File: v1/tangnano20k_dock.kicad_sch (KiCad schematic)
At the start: 42 parts, among them J1 Mini-DIN-6, J2 2x20 Pin Female, J3 Conn_01x03_Male, J4 Conn_01x20, J5 Conn_01x02, J6 RCA, J7 FCR684205T, J8 AudioJack3, U1 TXS0104E, U2 TangNano20K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

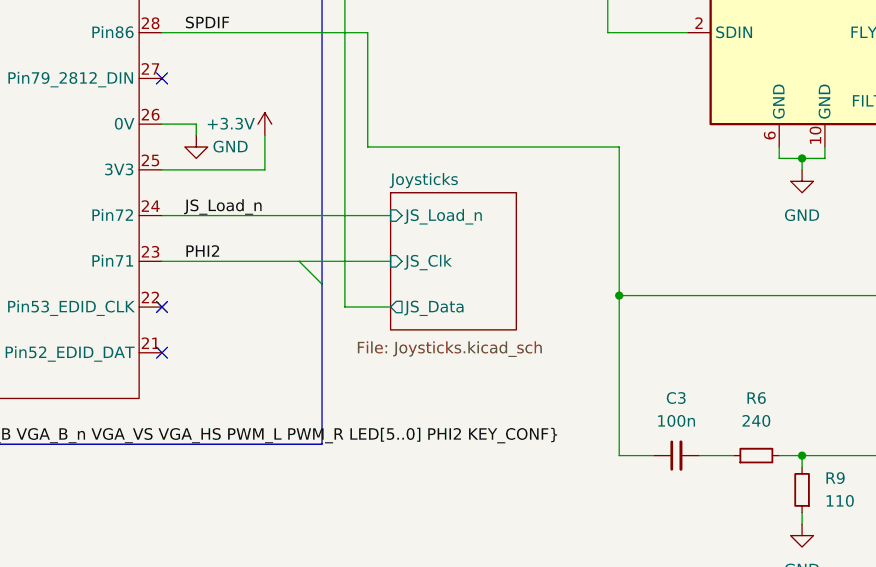
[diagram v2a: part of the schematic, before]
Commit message: Add an RC filter to allow PHI2 clock edge to be slowed to avoid ringing
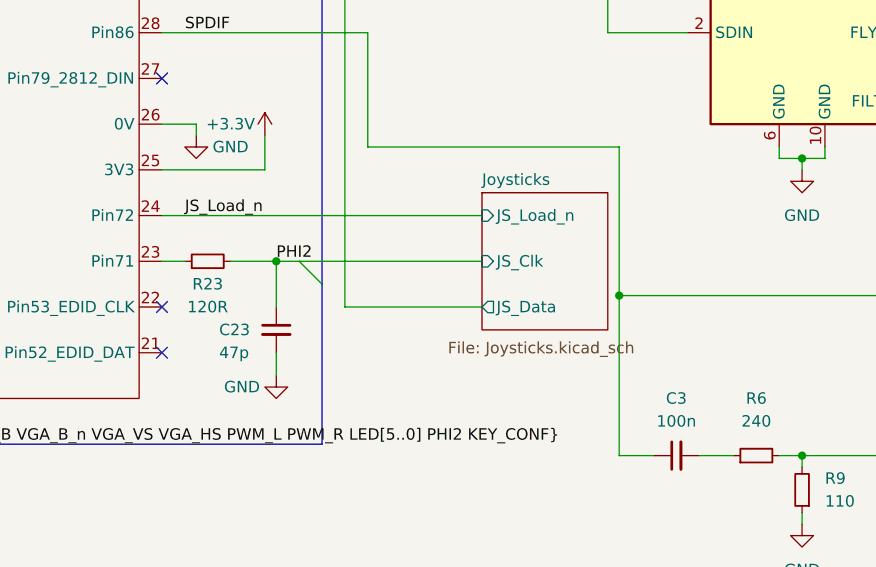
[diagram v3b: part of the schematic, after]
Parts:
- added C23: 47p, Capacitor_SMD:C_1206_3216Metric_Pad1.33x1.80mm_HandSolder, symbol Device:C_Small
- added R23: 120R, Resistor_SMD:R_1206_3216Metric_Pad1.30x1.75mm_HandSolder, symbol Device:R_Small
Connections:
- net GND: now also C23.2
- net PHI2: now also C23.1, R23.2; no longer U2.23 (Pin71)
- new net: R23.1, U2.23 (Pin71)
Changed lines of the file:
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@@
   (junction (at 250.19 73.66) (diameter 0) (color 0 0 0 0)
   )
+  (junction (at 173.99 130.81) (diameter 0) (color 0 0 0 0)
+  )
   (junction (at 107.95 151.13) (diameter 0) (color 0 0 0 0)
   )
@@
     (stroke (width 0) (type default) (color 0 0 0 0))
   )
+  (wire (pts (xy 161.29 130.81) (xy 163.83 130.81))
+    (stroke (width 0) (type default) (color 0 0 0 0))
+  )
   (wire (pts (xy 267.97 144.78) (xy 267.97 146.05))
     (stroke (width 0) (type default) (color 0 0 0 0))
@@
     (stroke (width 0) (type default) (color 0 0 0 0))
   )
-  (wire (pts (xy 181.61 135.89) (xy 186.69 135.89))
+  (wire (pts (xy 181.61 135.89) (xy 196.85 135.89))
     (stroke (width 0) (type default) (color 0 0 0 0))
   )
@@
     (stroke (width 0) (type default) (color 0 0 0 0))
   )
-  (wire (pts (xy 161.29 130.81) (xy 176.53 130.81))
-    (stroke (width 0) (type default) (color 0 0 0 0))
-  )
   (bus (pts (xy 39.37 97.79) (xy 39.37 100.33))
     (stroke (width 0) (type default) (color 0 0 0 0))
@@
     (stroke (width 0) (type default) (color 0 0 0 0))
   )
-  (wire (pts (xy 176.53 130.81) (xy 186.69 130.81))
+  (wire (pts (xy 176.53 130.81) (xy 196.85 130.81))
     (stroke (width 0) (type default) (color 0 0 0 0))
   )
@@
     (stroke (width 0) (type default) (color 0 0 0 0))
   )
+  (wire (pts (xy 168.91 130.81) (xy 173.99 130.81))
+    (stroke (width 0) (type default) (color 0 0 0 0))
+  )
   (wire (pts (xy 64.77 85.09) (xy 54.61 85.09))
     (stroke (width 0) (type default) (color 0 0 0 0))
@@
     (stroke (width 0) (type default) (color 0 0 0 0))
   )
+  (wire (pts (xy 173.99 140.97) (xy 173.99 143.51))
+    (stroke (width 0) (type default) (color 0 0 0 0))
+  )
   (wire (pts (xy 250.19 67.31) (xy 250.19 66.04))
     (stroke (width 0) (type default) (color 0 0 0 0))
@@
     (stroke (width 0) (type default) (color 0 0 0 0))
   )
+  (wire (pts (xy 173.99 135.89) (xy 173.99 130.81))
+    (stroke (width 0) (type default) (color 0 0 0 0))
+  )
   (wire (pts (xy 212.09 152.4) (xy 215.9 152.4))
     (stroke (width 0) (type default) (color 0 0 0 0))
@@
     (stroke (width 0) (type default) (color 0 0 0 0))
   )
+  (wire (pts (xy 173.99 130.81) (xy 176.53 130.81))
+    (stroke (width 0) (type default) (color 0 0 0 0))
+  )
   (bus (pts (xy 107.95 118.11) (xy 107.95 123.19))
     (stroke (width 0) (type default) (color 0 0 0 0))
@@
     (stroke (width 0) (type default) (color 0 0 0 0))
   )
-  (wire (pts (xy 161.29 125.73) (xy 186.69 125.73))
+  (wire (pts (xy 161.29 125.73) (xy 196.85 125.73))
     (stroke (width 0) (type default) (color 0 0 0 0))
   )
@@
     (effects (font (size 1.27 1.27)) (justify left bottom))
   )
-  (label "PHI2" (at 163.83 130.81 0)
+  (label "PHI2" (at 173.99 130.81 0)
     (effects (font (size 1.27 1.27)) (justify left bottom))
   )
@@
     (pin "2")
   )
+  (symbol (lib_id "Device:C_Small") (at 173.99 138.43 0) (unit 1)
+    (in_bom yes) (on_board yes)
+    (property "Reference" "C23" (id 0) (at 167.64 138.43 0)
+      (effects (font (size 1.27 1.27)) (justify left))
+    )
+    (property "Value" "47p" (id 1) (at 167.64 140.97 0)
+      (effects (font (size 1.27 1.27)) (justify left))
+    )
+    (property "Footprint" "Capacitor_SMD:C_1206_3216Metric_Pad1.33x1.80mm_HandSolder" (id 2) (at 173.99 138.43 0)
+      (effects (font (size 1.27 1.27)) hide)
+    )
+    (property "Datasheet" "~" (id 3) (at 173.99 138.43 0)
+      (effects (font (size 1.27 1.27)) hide)
+    )
+    (pin "1")
+    (pin "2")
+  )
   (symbol (lib_id "Device:C_Small") (at 74.93 19.05 0) (mirror x) (unit 1)
     (in_bom yes) (on_board yes)
@@
     (pin "1")
   )
+  (symbol (lib_id "Device:R_Small") (at 166.37 130.81 90) (unit 1)
+    (in_bom yes) (on_board yes)
+    (property "Reference" "R23" (id 0) (at 166.37 133.35 90))
+    (property "Value" "120R" (id 1) (at 166.37 135.89 90))
+    (property "Footprint" "Resistor_SMD:R_1206_3216Metric_Pad1.30x1.75mm_HandSolder" (id 2) (at 166.37 130.81 0)
+      (effects (font (size 1.27 1.27)) hide)
+    )
+    (property "Datasheet" "~" (id 3) (at 166.37 130.81 0)
+      (effects (font (size 1.27 1.27)) hide)
+    )
+    (pin "1")
+    (pin "2")
+  )
   (symbol (lib_id "power:GND") (at 232.41 120.65 0) (unit 1)
     (in_bom yes) (on_board yes) (fields_autoplaced)
@@
     (pin "3")
   )
+  (symbol (lib_id "power:GND") (at 173.99 143.51 0) (unit 1)
+    (in_bom yes) (on_board yes)
+    (property "Reference" "#PWR0101" (id 0) (at 173.99 149.86 0)
+      (effects (font (size 1.27 1.27)) hide)
+    )
+    (property "Value" "GND" (id 1) (at 170.18 144.78 0))
+    (property "Footprint" "" (id 2) (at 173.99 143.51 0)
+      (effects (font (size 1.27 1.27)) hide)
+    )
+    (property "Datasheet" "" (id 3) (at 173.99 143.51 0)
+      (effects (font (size 1.27 1.27)) hide)
+    )
+    (pin "1")
+  )
   (symbol (lib_id "Mechanical:MountingHole") (at 185.42 34.29 0) (unit 1)
     (in_bom yes) (on_board yes) (fields_autoplaced)
@@
     (pin "1")
   )
-  (sheet (at 186.69 123.19) (size 13.97 15.24)
+  (sheet (at 196.85 123.19) (size 13.97 15.24)
     (stroke (width 0.1524) (type solid) (color 0 0 0 0))
     (fill (color 0 0 0 0.0000))
-    (property "Sheet name" "Joysticks" (id 0) (at 186.69 122.4784 0)
+    (property "Sheet name" "Joysticks" (id 0) (at 196.85 122.4784 0)
       (effects (font (size 1.27 1.27)) (justify left bottom))
     )
-    (property "Sheet file" "Joysticks.kicad_sch" (id 1) (at 182.88 139.7 0)
+    (property "Sheet file" "Joysticks.kicad_sch" (id 1) (at 193.04 139.7 0)
       (effects (font (size 1.27 1.27)) (justify left top))
     )
-    (pin "JS_Data" output (at 186.69 135.89 180)
+    (pin "JS_Data" output (at 196.85 135.89 180)
       (effects (font (size 1.27 1.27)) (justify left))
     )
-    (pin "JS_Load_n" input (at 186.69 125.73 180)
+    (pin "JS_Load_n" input (at 196.85 125.73 180)
       (effects (font (size 1.27 1.27)) (justify left))
     )
-    (pin "JS_Clk" input (at 186.69 130.81 180)
+    (pin "JS_Clk" input (at 196.85 130.81 180)
       (effects (font (size 1.27 1.27)) (justify left))
     )
@@
       (reference "#PWR055") (unit 1) (value "GND") (footprint "")
     )
+    (path "/7eb3d7a6-25d3-48be-8262-4dda673731da"
+      (reference "#PWR0101") (unit 1) (value "GND") (footprint "")
+    )
     (path "/1fd682e2-38d3-4e6f-9b3a-e87d3b2b467c"
       (reference "C1") (unit 1) (value "100n") (footprint "Capacitor_SMD:C_1206_3216Metric_Pad1.33x1.80mm_HandSolder")
@@
       (reference "C22") (unit 1) (value "100n") (footprint "Capacitor_SMD:C_1206_3216Metric_Pad1.33x1.80mm_HandSolder")
     )
+    (path "/1b77f8d4-06d7-4df1-a443-7f89e552bd40"
+      (reference "C23") (unit 1) (value "47p") (footprint "Capacitor_SMD:C_1206_3216Metric_Pad1.33x1.80mm_HandSolder")
+    )
     (path "/3efa4c66-1bea-40a4-bda9-02b28c07af29"
       (reference "H1") (unit 1) (value "MountingHole") (footprint "TangNano20k:MountingHole_3.2mm_M3")
@@
       (reference "R22") (unit 1) (value "100") (footprint "Resistor_SMD:R_1206_3216Metric_Pad1.30x1.75mm_HandSolder")
     )
+    (path "/21ede51c-808e-4d97-ae44-af346bb9dd2e"
+      (reference "R23") (unit 1) (value "120R") (footprint "Resistor_SMD:R_1206_3216Metric_Pad1.30x1.75mm_HandSolder")
+    )
     (path "/0331ec4d-b3bf-4145-9efb-ad1204df77fa/8258306a-00ac-4756-af11-954dcf664468"

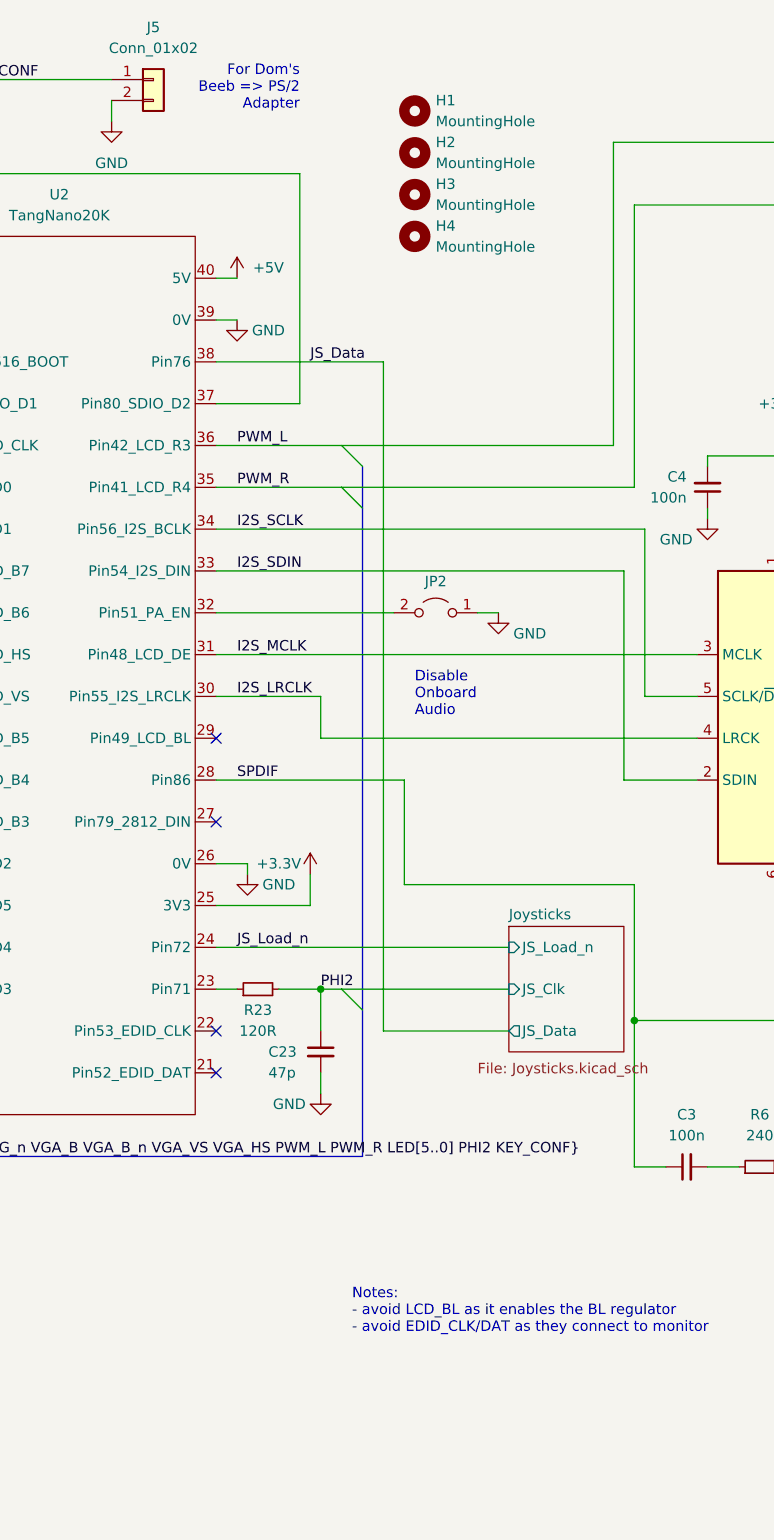
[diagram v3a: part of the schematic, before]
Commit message: Added Cliff DC10A power jack + schottky diode
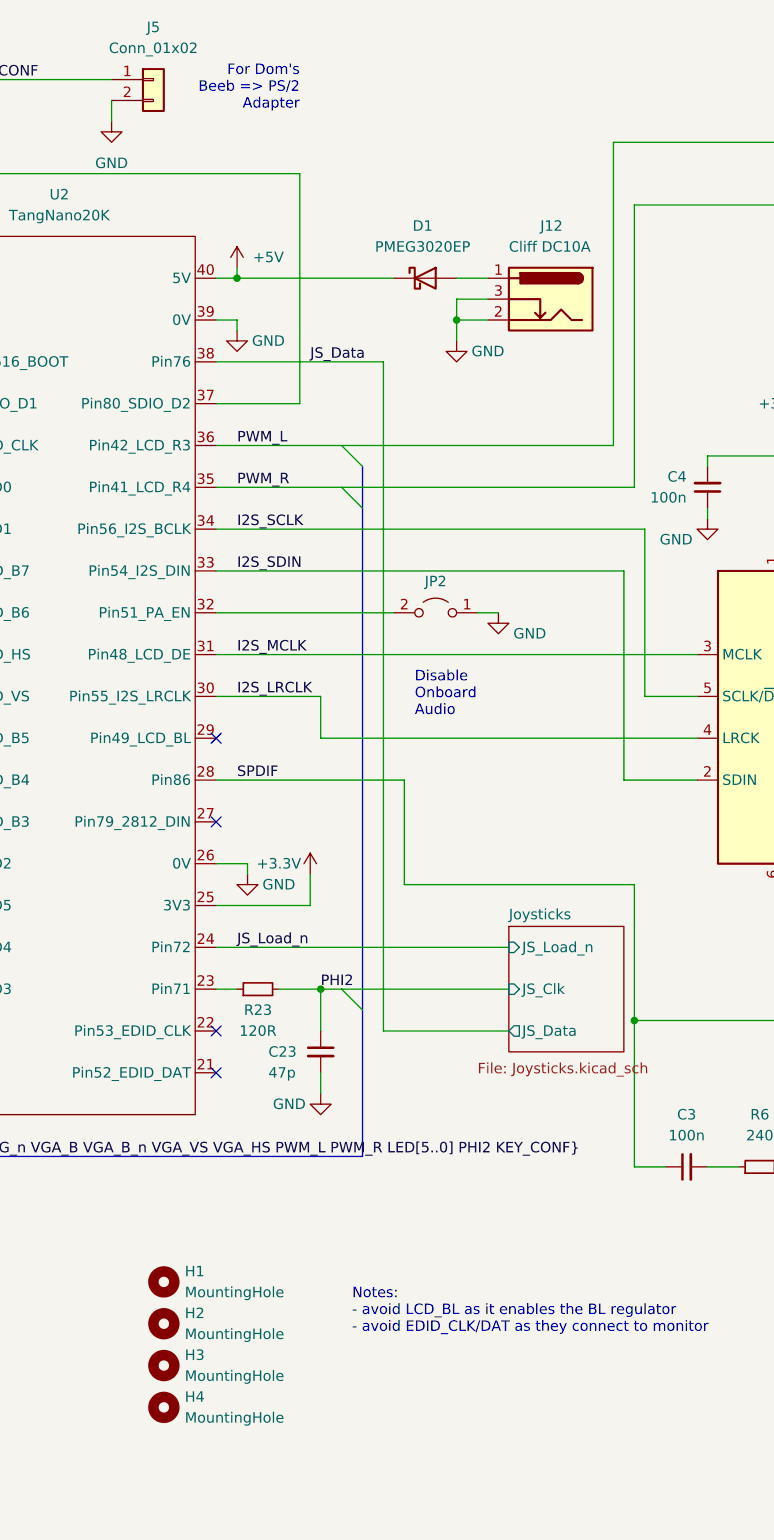
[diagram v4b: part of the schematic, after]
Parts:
- added D1: PMEG3020EP, Diode_SMD:D_SOD-128, symbol Device:D_Schottky
- added J12: Cliff DC10A, TangNano20k:CLIFF_FC68148_DC10A, symbol Connector:Barrel_Jack_Switch
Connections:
- net +5V: now also D1.1 (K)
- net GND: now also J12.2, J12.3
- new net: D1.2 (A), J12.1
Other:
- moved on the sheet: H1, H2, H3, H4

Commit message: More minor DFM issues
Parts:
- D1: footprint Diode_SMD:D_SOD-128 -> TangNano20k:D_SOD-128
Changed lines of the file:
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@@
     (property "Reference" "D1" (id 0) (at 186.3725 38.1 0))
     (property "Value" "PMEG3020EP" (id 1) (at 186.3725 40.64 0))
-    (property "Footprint" "Diode_SMD:D_SOD-128" (id 2) (at 186.69 44.45 0)
+    (property "Footprint" "TangNano20k:D_SOD-128" (id 2) (at 186.69 44.45 0)
       (effects (font (size 1.27 1.27)) hide)
     )
@@
     )
     (path "/23e0812c-8650-479d-a1a6-e0d5388e06e9"
-      (reference "D1") (unit 1) (value "PMEG3020EP") (footprint "Diode_SMD:D_SOD-128")
+      (reference "D1") (unit 1) (value "PMEG3020EP") (footprint "TangNano20k:D_SOD-128")
     )
     (path "/3efa4c66-1bea-40a4-bda9-02b28c07af29"

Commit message: Update resistor values and refresh PDF
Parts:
- R1, R2, R3, R4: value 390 -> 330
- R23: value 120R -> 100R
- R5: value 10K -> 3K3
- R6: value 240 -> 243
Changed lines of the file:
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@@
       (effects (font (size 1.27 1.27)) (justify left))
     )
-    (property "Value" "10K" (id 1) (at 109.22 26.6699 0)
+    (property "Value" "3K3" (id 1) (at 109.22 26.6699 0)
       (effects (font (size 1.27 1.27)) (justify left))
     )
@@
     (in_bom yes) (on_board yes)
     (property "Reference" "R23" (id 0) (at 166.37 133.35 90))
-    (property "Value" "120R" (id 1) (at 166.37 135.89 90))
+    (property "Value" "100R" (id 1) (at 166.37 135.89 90))
     (property "Footprint" "Resistor_SMD:R_1206_3216Metric_Pad1.30x1.75mm_HandSolder" (id 2) (at 166.37 130.81 0)
       (effects (font (size 1.27 1.27)) hide)
@@
     (in_bom yes) (on_board yes) (fields_autoplaced)
     (property "Reference" "R6" (id 0) (at 227.33 146.05 90))
-    (property "Value" "240" (id 1) (at 227.33 148.59 90))
+    (property "Value" "243" (id 1) (at 227.33 148.59 90))
     (property "Footprint" "Resistor_SMD:R_1206_3216Metric_Pad1.30x1.75mm_HandSolder" (id 2) (at 227.33 152.4 0)
       (effects (font (size 1.27 1.27)) hide)
@@
     (in_bom yes) (on_board yes)
     (property "Reference" "R1" (id 0) (at 50.8 26.67 90))
-    (property "Value" "390" (id 1) (at 50.8 21.59 90))
+    (property "Value" "330" (id 1) (at 50.8 21.59 90))
     (property "Footprint" "Resistor_SMD:R_1206_3216Metric_Pad1.30x1.75mm_HandSolder" (id 2) (at 50.8 24.13 0)
       (effects (font (size 1.27 1.27)) hide)
@@
     (in_bom yes) (on_board yes)
     (property "Reference" "R4" (id 0) (at 50.8 62.23 90))
-    (property "Value" "390" (id 1) (at 50.8 57.15 90))
+    (property "Value" "330" (id 1) (at 50.8 57.15 90))
     (property "Footprint" "Resistor_SMD:R_1206_3216Metric_Pad1.30x1.75mm_HandSolder" (id 2) (at 50.8 59.69 0)
       (effects (font (size 1.27 1.27)) hide)
@@
     (in_bom yes) (on_board yes)
     (property "Reference" "R3" (id 0) (at 50.8 54.61 90))
-    (property "Value" "390" (id 1) (at 50.8 49.53 90))
+    (property "Value" "330" (id 1) (at 50.8 49.53 90))
     (property "Footprint" "Resistor_SMD:R_1206_3216Metric_Pad1.30x1.75mm_HandSolder" (id 2) (at 50.8 52.07 0)
       (effects (font (size 1.27 1.27)) hide)
@@
     (in_bom yes) (on_board yes)
     (property "Reference" "R2" (id 0) (at 50.8 34.29 90))
-    (property "Value" "390" (id 1) (at 50.8 29.21 90))
+    (property "Value" "330" (id 1) (at 50.8 29.21 90))
     (property "Footprint" "Resistor_SMD:R_1206_3216Metric_Pad1.30x1.75mm_HandSolder" (id 2) (at 50.8 31.75 0)
       (effects (font (size 1.27 1.27)) hide)
@@
     )
     (path "/4dc74927-f9a9-448a-9b80-6c4062674486"
-      (reference "R1") (unit 1) (value "390") (footprint "Resistor_SMD:R_1206_3216Metric_Pad1.30x1.75mm_HandSolder")
+      (reference "R1") (unit 1) (value "330") (footprint "Resistor_SMD:R_1206_3216Metric_Pad1.30x1.75mm_HandSolder")
     )
     (path "/d9474aa6-7130-4a20-8e60-ca64b8599c1b"
-      (reference "R2") (unit 1) (value "390") (footprint "Resistor_SMD:R_1206_3216Metric_Pad1.30x1.75mm_HandSolder")
+      (reference "R2") (unit 1) (value "330") (footprint "Resistor_SMD:R_1206_3216Metric_Pad1.30x1.75mm_HandSolder")
     )
     (path "/a2d110ca-0bfc-4aec-8893-85fc43a7e042"
-      (reference "R3") (unit 1) (value "390") (footprint "Resistor_SMD:R_1206_3216Metric_Pad1.30x1.75mm_HandSolder")
+      (reference "R3") (unit 1) (value "330") (footprint "Resistor_SMD:R_1206_3216Metric_Pad1.30x1.75mm_HandSolder")
     )
     (path "/762d4812-bd8c-402c-94c0-48656fb4b616"
-      (reference "R4") (unit 1) (value "390") (footprint "Resistor_SMD:R_1206_3216Metric_Pad1.30x1.75mm_HandSolder")
+      (reference "R4") (unit 1) (value "330") (footprint "Resistor_SMD:R_1206_3216Metric_Pad1.30x1.75mm_HandSolder")
     )
     (path "/02e005ab-d466-403f-a516-098fae9061ff"
-      (reference "R5") (unit 1) (value "10K") (footprint "Resistor_SMD:R_1206_3216Metric_Pad1.30x1.75mm_HandSolder")
+      (reference "R5") (unit 1) (value "3K3") (footprint "Resistor_SMD:R_1206_3216Metric_Pad1.30x1.75mm_HandSolder")
     )
     (path "/32b9a4f2-c13f-445f-b4d7-18e41668057c"
-      (reference "R6") (unit 1) (value "240") (footprint "Resistor_SMD:R_1206_3216Metric_Pad1.30x1.75mm_HandSolder")
+      (reference "R6") (unit 1) (value "243") (footprint "Resistor_SMD:R_1206_3216Metric_Pad1.30x1.75mm_HandSolder")
     )
     (path "/c775bc63-159c-4669-b08c-31df3fc83a7c"
@@
     )
     (path "/21ede51c-808e-4d97-ae44-af346bb9dd2e"
-      (reference "R23") (unit 1) (value "120R") (footprint "Resistor_SMD:R_1206_3216Metric_Pad1.30x1.75mm_HandSolder")
+      (reference "R23") (unit 1) (value "100R") (footprint "Resistor_SMD:R_1206_3216Metric_Pad1.30x1.75mm_HandSolder")
     )
     (path "/0331ec4d-b3bf-4145-9efb-ad1204df77fa/8258306a-00ac-4756-af11-954dcf664468"
